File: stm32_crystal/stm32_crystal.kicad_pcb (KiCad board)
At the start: 2 copper layers, 21 parts, among them U1 STM32F103C6Tx

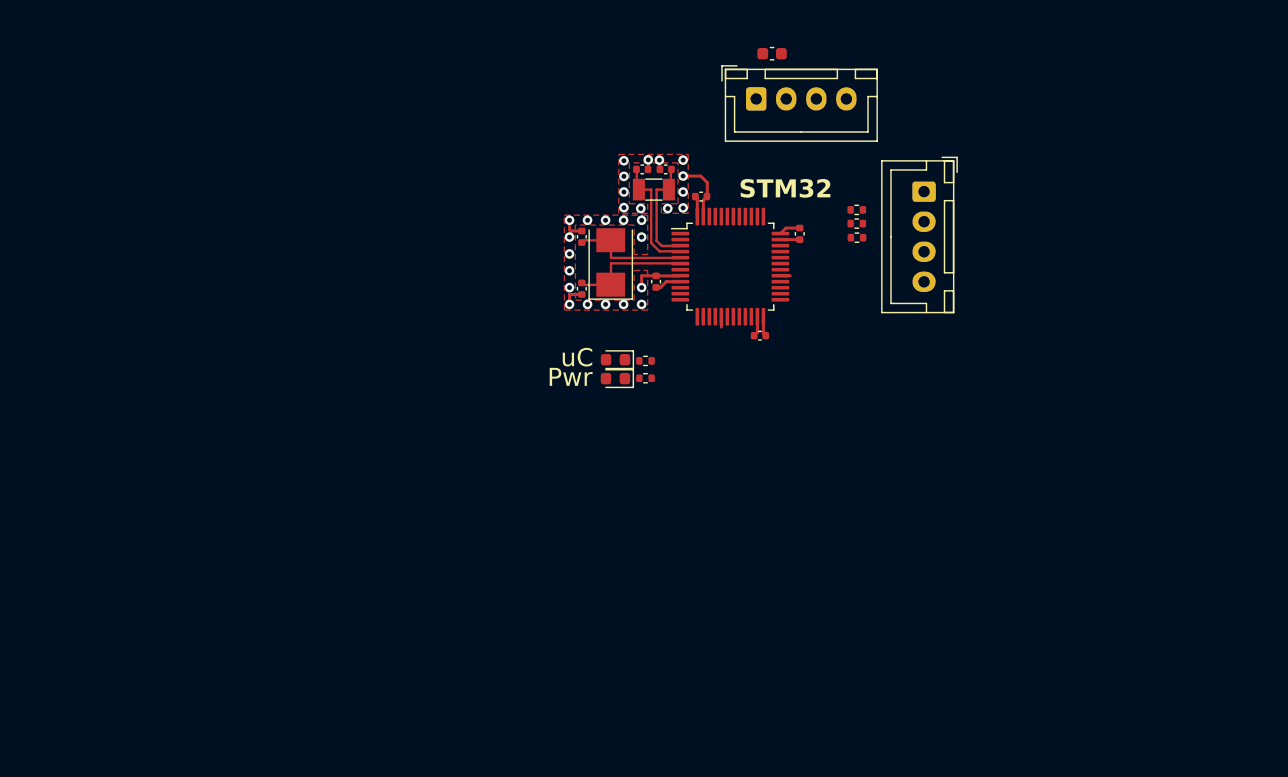
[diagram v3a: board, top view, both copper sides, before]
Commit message: fix layout stm32
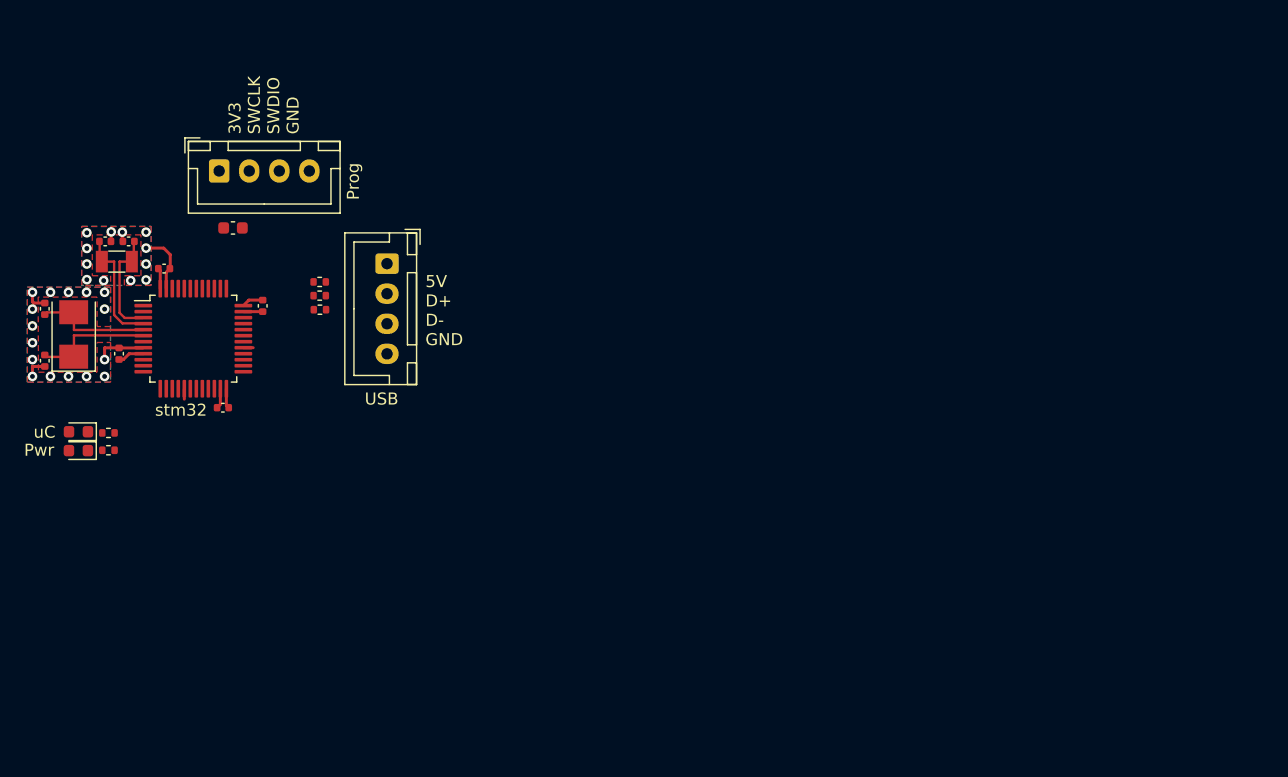
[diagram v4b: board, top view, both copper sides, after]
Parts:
- moved Prog_C1 47.1 mm to (135.4, 92.5)
- moved RTC_C2 45.1 mm to (126.7, 93.6)
- moved U1 45.1 mm to (132.1, 101.7)
- moved USB_R2 45.1 mm to (142.6, 99.3)
- moved Vdd4 45.1 mm to (129.6, 95.9)
- moved LED_R1 45.1 mm to (125.0, 109.5)
- moved LED_R2 45.1 mm to (125.0, 111.0)
- moved PWR_LED1 45.1 mm to (122.5, 111.0)
- moved RTC_C1 45.1 mm to (124.7, 93.6)
- moved RTC_Y1 45.1 mm to (125.7, 95.3)
- moved Vdd2 45.1 mm to (125.9, 102.9)
- moved uC_LED1 45.1 mm to (122.5, 109.4)
- moved CC1 45.1 mm to (119.7, 99.2)
- moved CC2 45.1 mm to (119.7, 103.5)
- moved Prog1 45.1 mm to (134.2, 87.7)
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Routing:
- added copper zone on B.Cu, net GND
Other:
- board text added: "3V3 SWCLK SWDIO GND"
- board text added: "5V D+ D- GND"
- board text added: "Prog"
- board text added: "USB"
- board text added: "stm32"
- board text removed: "STM32"
